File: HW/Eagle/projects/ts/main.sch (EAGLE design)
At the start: 43 parts, among them IC1 4050D, T1 IRLML2502, T2 IRLML2502, U1 ATMEGA328P-PU, U2 LM2576T, U3 HT7533, U4 LM75

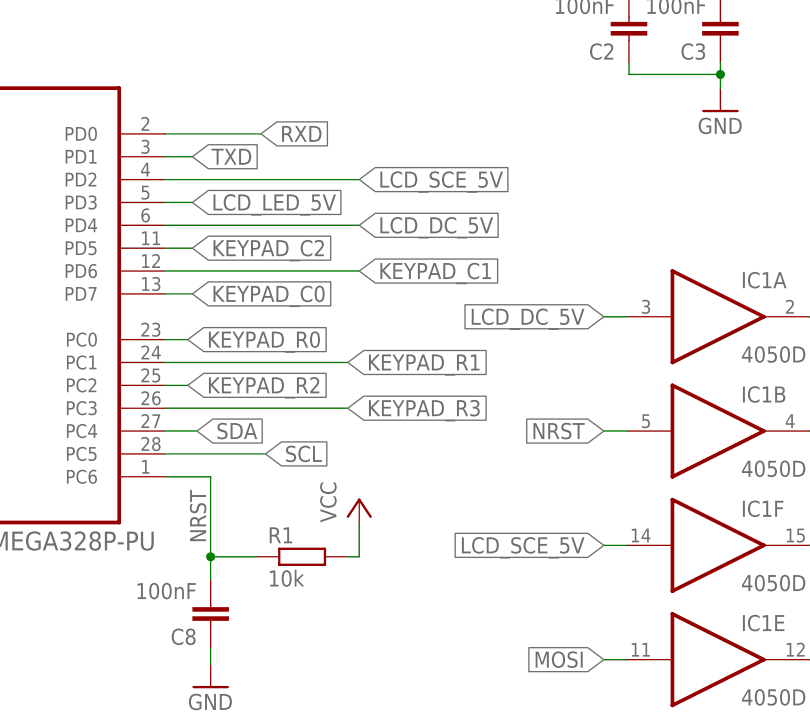
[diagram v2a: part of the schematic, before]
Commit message: Swaped LCD_SCE_5V and LCD_DC_5V signals on 4050
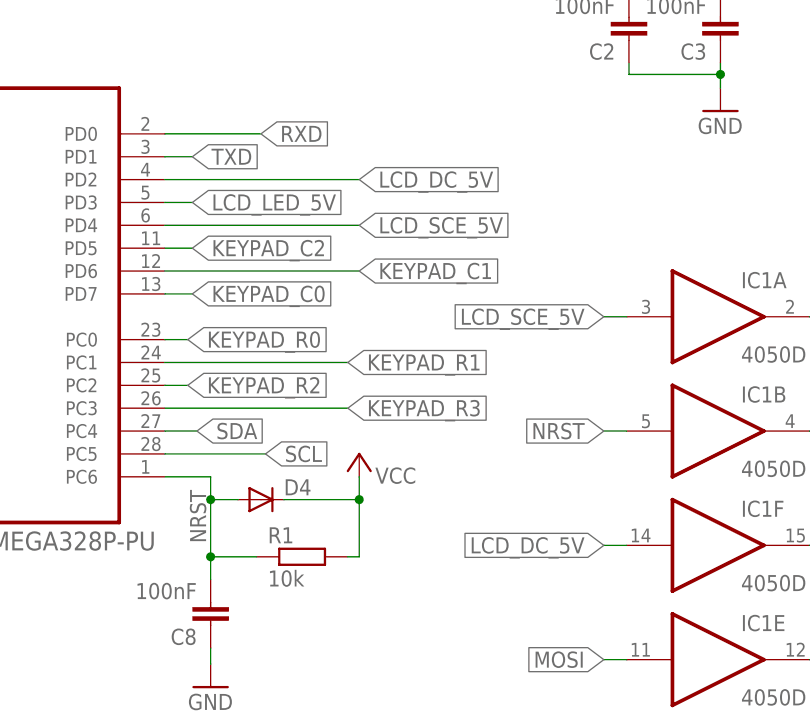
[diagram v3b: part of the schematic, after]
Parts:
- added D4: (no value), diode:DIODE-MINIMELF
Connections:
- net LCD_DC_5V: now also IC1F.I, U1.PD2; no longer IC1A.I, U1.PD4
- net LCD_SCE_5V: now also IC1A.I, U1.PD4; no longer IC1F.I, U1.PD2
- net NRST: now also D4.A
- net VCC: now also D4.C
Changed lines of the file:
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@@
 <part name="P+11" library="supply1" deviceset="+12V" device=""/>
 <part name="P+12" library="supply1" deviceset="+12V" device=""/>
+<part name="D4" library="diode" deviceset="DIODE-" device="MINIMELF"/>
 </parts>
 <sheets>
@@
 <instance part="C4" gate="G$1" x="80.01" y="66.294" rot="R180"/>
 <instance part="C5" gate="G$1" x="87.884" y="66.294" rot="R180"/>
-<instance part="P+3" gate="VCC" x="160.782" y="63.5"/>
+<instance part="P+3" gate="VCC" x="160.782" y="68.58" smashed="yes">
+<attribute name="VALUE" x="162.56" y="65.278" size="1.778" layer="96"/>
+</instance>
 <instance part="R1" gate="G$1" x="154.432" y="57.15"/>
 <instance part="R2" gate="G$1" x="96.012" y="69.85" rot="R180"/>
@@
 <attribute name="VALUE" x="50.8" y="119.38" size="1.778" layer="96"/>
 </instance>
+<instance part="D4" gate="G$1" x="149.86" y="63.5"/>
 </instances>
 <busses>
@@
 <pinref part="P+3" gate="VCC" pin="VCC"/>
 <wire x1="159.512" y1="57.15" x2="160.782" y2="57.15" width="0.1524" layer="91"/>
-<wire x1="160.782" y1="57.15" x2="160.782" y2="60.96" width="0.1524" layer="91"/>
+<wire x1="160.782" y1="57.15" x2="160.782" y2="63.5" width="0.1524" layer="91"/>
+<pinref part="D4" gate="G$1" pin="C"/>
+<wire x1="160.782" y1="63.5" x2="160.782" y2="66.04" width="0.1524" layer="91"/>
+<wire x1="152.4" y1="63.5" x2="160.782" y2="63.5" width="0.1524" layer="91"/>
+<junction x="160.782" y="63.5"/>
 </segment>
 <segment>
@@
 <pinref part="R1" gate="G$1" pin="1"/>
 <wire x1="149.352" y1="57.15" x2="144.272" y2="57.15" width="0.1524" layer="91"/>
-<wire x1="144.272" y1="57.15" x2="144.272" y2="66.04" width="0.1524" layer="91"/>
+<wire x1="144.272" y1="57.15" x2="144.272" y2="63.5" width="0.1524" layer="91"/>
 <pinref part="U1" gate="A" pin="PC6"/>
+<wire x1="144.272" y1="63.5" x2="144.272" y2="66.04" width="0.1524" layer="91"/>
 <wire x1="144.272" y1="66.04" x2="139.192" y2="66.04" width="0.1524" layer="91"/>
 <label x="143.764" y="58.674" size="1.778" layer="95" rot="R90"/>
@@
 <wire x1="144.272" y1="57.15" x2="144.272" y2="54.61" width="0.1524" layer="91"/>
 <junction x="144.272" y="57.15"/>
+<pinref part="D4" gate="G$1" pin="A"/>
+<wire x1="147.32" y1="63.5" x2="144.272" y2="63.5" width="0.1524" layer="91"/>
+<junction x="144.272" y="63.5"/>
 </segment>
 <segment>
@@
 <net name="LCD_SCE_5V" class="0">
 <segment>
+<pinref part="U1" gate="A" pin="PD4"/>
+<wire x1="139.192" y1="93.98" x2="160.782" y2="93.98" width="0.1524" layer="91"/>
+<label x="160.782" y="93.98" size="1.778" layer="95" xref="yes"/>
+</segment>
+<segment>
+<pinref part="IC1" gate="A" pin="I"/>
+<wire x1="190.5" y1="83.82" x2="187.96" y2="83.82" width="0.1524" layer="91"/>
+<label x="187.96" y="83.82" size="1.778" layer="95" rot="R180" xref="yes"/>
+</segment>
+</net>
+<net name="LCD_DC_5V" class="0">
+<segment>
 <pinref part="U1" gate="A" pin="PD2"/>
 <wire x1="139.192" y1="99.06" x2="160.782" y2="99.06" width="0.1524" layer="91"/>
@@
 </segment>
 </net>
-<net name="LCD_DC_5V" class="0">
-<segment>
-<pinref part="U1" gate="A" pin="PD4"/>
-<wire x1="139.192" y1="93.98" x2="160.782" y2="93.98" width="0.1524" layer="91"/>
-<label x="160.782" y="93.98" size="1.778" layer="95" xref="yes"/>
-</segment>
-<segment>
-<pinref part="IC1" gate="A" pin="I"/>
-<wire x1="190.5" y1="83.82" x2="187.96" y2="83.82" width="0.1524" layer="91"/>
-<label x="187.96" y="83.82" size="1.778" layer="95" rot="R180" xref="yes"/>
-</segment>
-</net>

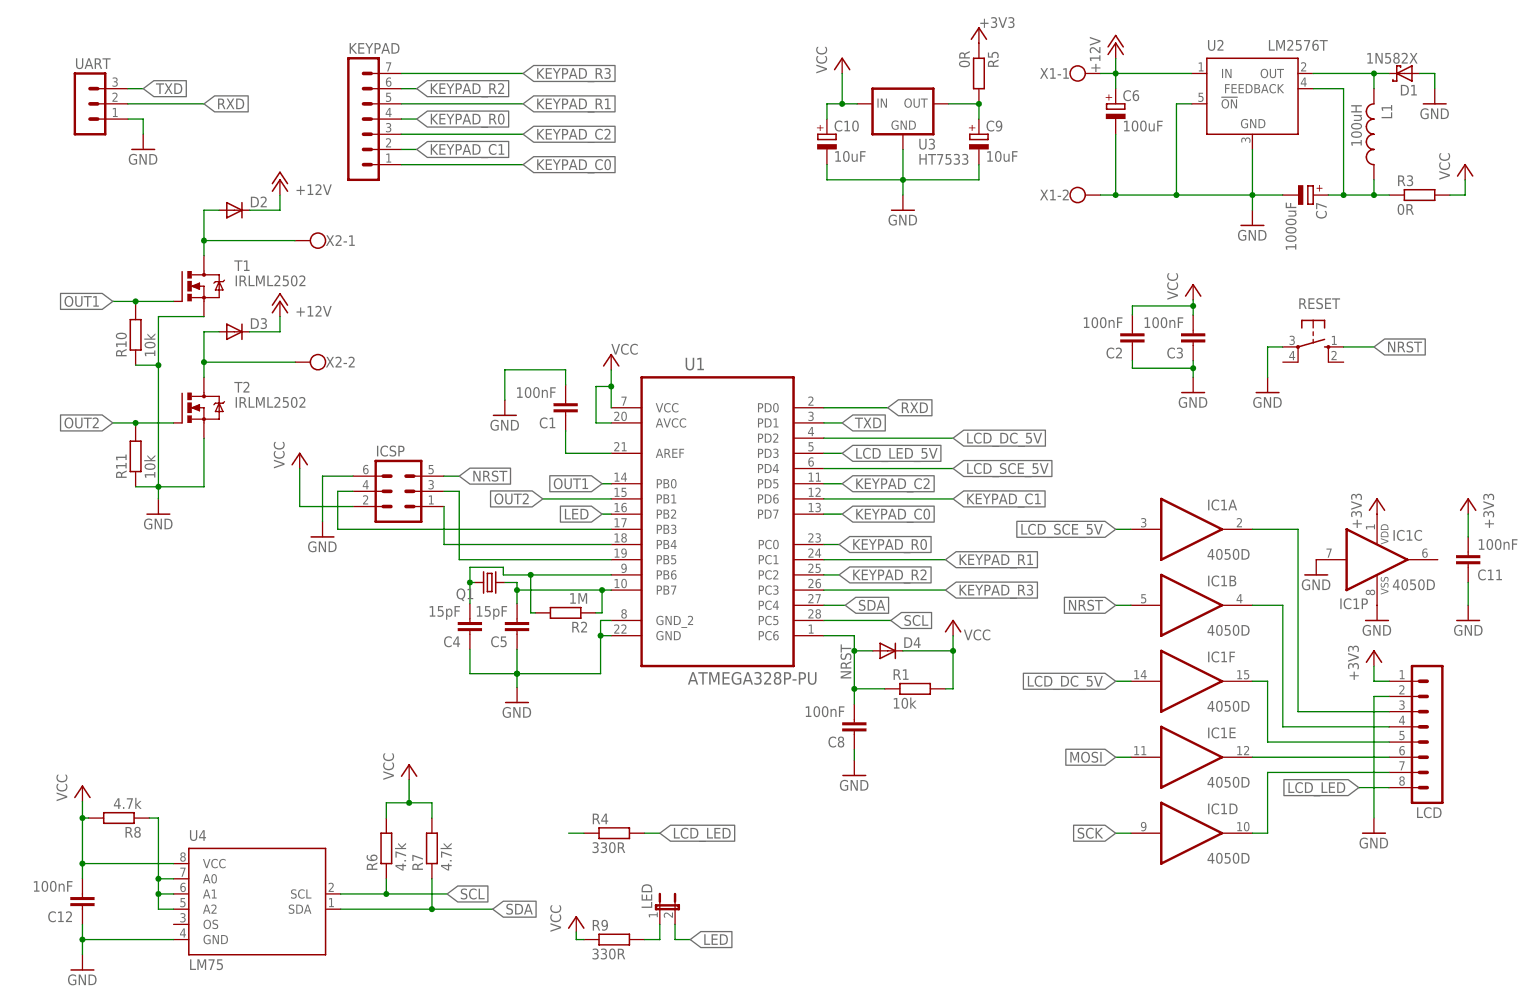
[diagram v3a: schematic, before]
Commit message: Added Power CMOS transistors
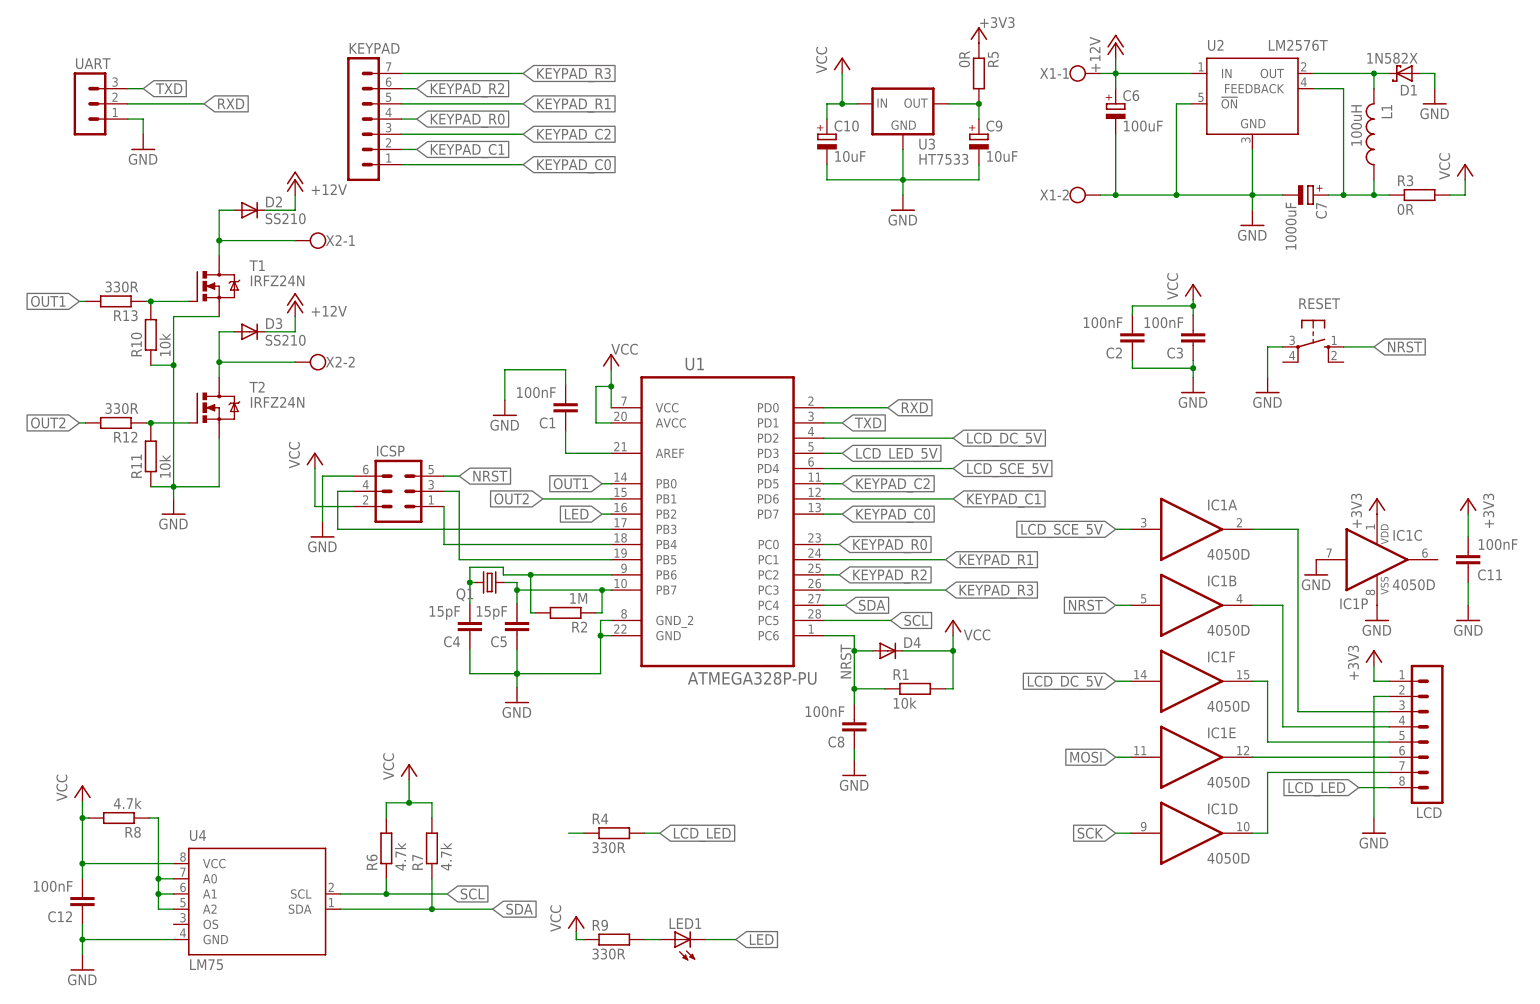
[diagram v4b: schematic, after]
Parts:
- removed LED: (no value), jumper:JP1E
- added LED1: (no value), led:LED3MM
- added R12, R13: 330R, rcl:R-EU_R0805
- D2, D3: value (none) -> SS210; device diode:DIODE-MINIMELF -> diode:DIODE-SMB
- T1, T2: value IRLML2502 -> IRFZ24N; device misc:IRLML2502 -> misc:IRFZ24N
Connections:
- new net N$12: R11.2, R12.1, T2.G
- new net N$9: R10.2, R13.1, T1.G
- net LED: now also LED1.C; no longer LED.2
- net N$6: now also LED1.A; no longer LED.1
- net OUT1: now also R13.2; no longer R10.2, T1.G
- net OUT2: now also R12.2; no longer R11.2, T2.G
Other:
- moved on the sheet: D2, D3, R10, R11, T1, T2

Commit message: HW Release 1
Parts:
- LED1: device led:LED3MM -> led:LED5MM
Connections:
- removed net N$2: R4.1
- net LCD_LED_5V: now also R4.1, U1.PB2; no longer U1.PD3
- net LED: now also U1.PB1; no longer U1.PB2
- net OUT2: now also U1.PD3; no longer U1.PB1
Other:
- moved on the sheet: ICSP, R4
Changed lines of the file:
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@@
 <part name="R12" library="rcl" deviceset="R-EU_" device="R0805" value="330R"/>
 <part name="R13" library="rcl" deviceset="R-EU_" device="R0805" value="330R"/>
-<part name="LED1" library="led" deviceset="LED" device="3MM"/>
+<part name="LED1" library="led" deviceset="LED" device="5MM"/>
 </parts>
 <sheets>
@@
 <instance part="R1" gate="G$1" x="154.432" y="57.15"/>
 <instance part="R2" gate="G$1" x="96.012" y="69.85" rot="R180"/>
-<instance part="ICSP" gate="1" x="68.072" y="90.17"/>
-<instance part="P+4" gate="VCC" x="54.102" y="96.52"/>
-<instance part="GND4" gate="1" x="55.372" y="82.55"/>
+<instance part="ICSP" gate="1" x="62.992" y="90.17"/>
+<instance part="P+4" gate="VCC" x="49.022" y="96.52"/>
+<instance part="GND4" gate="1" x="50.292" y="82.55"/>
 <instance part="U2" gate="U" x="210.82" y="154.94"/>
 <instance part="FRAME1" gate="G$1" x="0" y="0"/>
@@
 <instance part="+3V4" gate="G$1" x="246.888" y="88.9" rot="MR0"/>
 <instance part="GND13" gate="1" x="246.888" y="68.58" rot="MR0"/>
-<instance part="R4" gate="G$1" x="104.14" y="33.02"/>
+<instance part="R4" gate="G$1" x="124.46" y="27.94"/>
 <instance part="RESET" gate="1" x="220.98" y="114.3" rot="R270"/>
 <instance part="GND14" gate="1" x="213.36" y="106.68"/>
@@
 <pinref part="ICSP" gate="1" pin="6"/>
 <pinref part="GND4" gate="1" pin="GND"/>
-<wire x1="60.452" y1="92.71" x2="55.372" y2="92.71" width="0.1524" layer="91"/>
-<wire x1="55.372" y1="92.71" x2="55.372" y2="85.09" width="0.1524" layer="91"/>
+<wire x1="55.372" y1="92.71" x2="50.292" y2="92.71" width="0.1524" layer="91"/>
+<wire x1="50.292" y1="92.71" x2="50.292" y2="85.09" width="0.1524" layer="91"/>
 </segment>
 <segment>
@@
 <pinref part="ICSP" gate="1" pin="2"/>
 <pinref part="P+4" gate="VCC" pin="VCC"/>
-<wire x1="60.452" y1="87.63" x2="54.102" y2="87.63" width="0.1524" layer="91"/>
-<wire x1="54.102" y1="87.63" x2="54.102" y2="93.98" width="0.1524" layer="91"/>
+<wire x1="55.372" y1="87.63" x2="49.022" y2="87.63" width="0.1524" layer="91"/>
+<wire x1="49.022" y1="87.63" x2="49.022" y2="93.98" width="0.1524" layer="91"/>
 </segment>
 <segment>
@@
 <segment>
 <pinref part="ICSP" gate="1" pin="1"/>
-<wire x1="103.632" y1="81.28" x2="75.692" y2="81.28" width="0.1524" layer="91"/>
-<wire x1="75.692" y1="81.28" x2="75.692" y2="87.63" width="0.1524" layer="91"/>
+<wire x1="103.632" y1="81.28" x2="70.612" y2="81.28" width="0.1524" layer="91"/>
+<wire x1="70.612" y1="81.28" x2="70.612" y2="87.63" width="0.1524" layer="91"/>
 <pinref part="U1" gate="A" pin="PB4"/>
+<label x="74.676" y="81.534" size="1.778" layer="95"/>
 </segment>
 </net>
@@
 <segment>
 <pinref part="ICSP" gate="1" pin="5"/>
-<wire x1="75.692" y1="92.71" x2="78.232" y2="92.71" width="0.1524" layer="91"/>
-<label x="78.232" y="92.71" size="1.778" layer="95" xref="yes"/>
+<wire x1="70.612" y1="92.71" x2="73.152" y2="92.71" width="0.1524" layer="91"/>
+<label x="73.152" y="92.71" size="1.778" layer="95" xref="yes"/>
 </segment>
 <segment>
@@
 <segment>
 <pinref part="ICSP" gate="1" pin="4"/>
-<wire x1="57.912" y1="83.82" x2="57.912" y2="90.17" width="0.1524" layer="91"/>
-<wire x1="57.912" y1="90.17" x2="60.452" y2="90.17" width="0.1524" layer="91"/>
+<wire x1="52.832" y1="83.82" x2="52.832" y2="90.17" width="0.1524" layer="91"/>
+<wire x1="52.832" y1="90.17" x2="55.372" y2="90.17" width="0.1524" layer="91"/>
 <pinref part="U1" gate="A" pin="PB3"/>
-<wire x1="103.632" y1="83.82" x2="57.912" y2="83.82" width="0.1524" layer="91"/>
+<wire x1="103.632" y1="83.82" x2="52.832" y2="83.82" width="0.1524" layer="91"/>
+<label x="74.676" y="84.074" size="1.778" layer="95"/>
 </segment>
 <segment>
@@
 <net name="SCK" class="0">
 <segment>
-<wire x1="78.232" y1="78.74" x2="78.232" y2="90.17" width="0.1524" layer="91"/>
+<wire x1="73.152" y1="78.74" x2="73.152" y2="90.17" width="0.1524" layer="91"/>
 <pinref part="ICSP" gate="1" pin="3"/>
-<wire x1="78.232" y1="90.17" x2="75.692" y2="90.17" width="0.1524" layer="91"/>
+<wire x1="73.152" y1="90.17" x2="70.612" y2="90.17" width="0.1524" layer="91"/>
 <pinref part="U1" gate="A" pin="PB5"/>
-<wire x1="103.632" y1="78.74" x2="78.232" y2="78.74" width="0.1524" layer="91"/>
+<wire x1="103.632" y1="78.74" x2="73.152" y2="78.74" width="0.1524" layer="91"/>
+<label x="74.676" y="78.994" size="1.778" layer="95"/>
 </segment>
 <segment>
@@
 <segment>
 <pinref part="R4" gate="G$1" pin="2"/>
-<wire x1="109.22" y1="33.02" x2="111.76" y2="33.02" width="0.1524" layer="91"/>
-<label x="111.76" y="33.02" size="1.778" layer="95" xref="yes"/>
+<wire x1="129.54" y1="27.94" x2="132.08" y2="27.94" width="0.1524" layer="91"/>
+<label x="132.08" y="27.94" size="1.778" layer="95" xref="yes"/>
 </segment>
 </net>
@@
 </segment>
 </net>
-<net name="N$2" class="0">
-<segment>
-<pinref part="R4" gate="G$1" pin="1"/>
-<wire x1="99.06" y1="33.02" x2="96.52" y2="33.02" width="0.1524" layer="91"/>
-</segment>
-</net>
 <net name="RXD" class="0">
 <segment>
@@
 <net name="LCD_LED_5V" class="0">
 <segment>
-<pinref part="U1" gate="A" pin="PD3"/>
-<wire x1="139.192" y1="96.52" x2="142.24" y2="96.52" width="0.1524" layer="91"/>
-<label x="142.24" y="96.52" size="1.778" layer="95" xref="yes"/>
+<pinref part="R4" gate="G$1" pin="1"/>
+<wire x1="119.38" y1="27.94" x2="116.84" y2="27.94" width="0.1524" layer="91"/>
+<label x="116.84" y="27.94" size="1.778" layer="95" rot="R180" xref="yes"/>
+</segment>
+<segment>
+<pinref part="U1" gate="A" pin="PB2"/>
+<wire x1="103.632" y1="86.36" x2="102.108" y2="86.36" width="0.1524" layer="91"/>
+<label x="102.108" y="86.36" size="1.778" layer="95" rot="R180" xref="yes"/>
 </segment>
 </net>
@@
 <net name="OUT2" class="0">
 <segment>
-<pinref part="U1" gate="A" pin="PB1"/>
-<wire x1="103.632" y1="88.9" x2="92.202" y2="88.9" width="0.1524" layer="91"/>
-<label x="92.202" y="88.9" size="1.778" layer="95" rot="R180" xref="yes"/>
-</segment>
-<segment>
 <pinref part="R12" gate="G$1" pin="2"/>
 <wire x1="15.748" y1="101.6" x2="14.732" y2="101.6" width="0.1524" layer="91"/>
 <label x="14.732" y="101.6" size="1.778" layer="95" rot="R180" xref="yes"/>
 </segment>
+<segment>
+<pinref part="U1" gate="A" pin="PD3"/>
+<wire x1="139.192" y1="96.52" x2="142.24" y2="96.52" width="0.1524" layer="91"/>
+<label x="142.24" y="96.52" size="1.778" layer="95" xref="yes"/>
+</segment>
 </net>
 <net name="LED" class="0">
-<segment>
-<pinref part="U1" gate="A" pin="PB2"/>
-<wire x1="103.632" y1="86.36" x2="102.108" y2="86.36" width="0.1524" layer="91"/>
-<label x="102.108" y="86.36" size="1.778" layer="95" rot="R180" xref="yes"/>
-</segment>
 <segment>
 <wire x1="119.38" y1="15.24" x2="124.46" y2="15.24" width="0.1524" layer="91"/>
@@
 <pinref part="LED1" gate="G$1" pin="C"/>
 </segment>
-</net>
+<segment>
+<pinref part="U1" gate="A" pin="PB1"/>
+<wire x1="103.632" y1="88.9" x2="82.042" y2="88.9" width="0.1524" layer="91"/>
+<label x="82.042" y="88.9" size="1.778" layer="95" rot="R180" xref="yes"/>
+</segment>
+</net>
